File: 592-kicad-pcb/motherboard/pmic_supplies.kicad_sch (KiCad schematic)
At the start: 0 parts

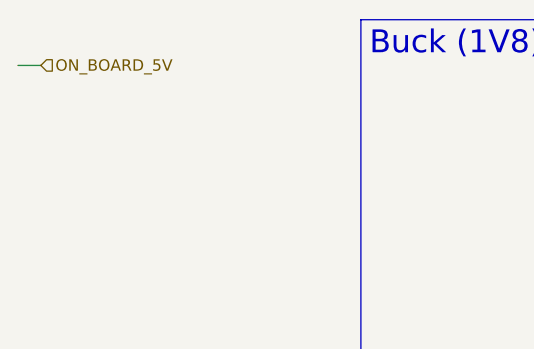
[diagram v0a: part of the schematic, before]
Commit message: pmic switching schem done
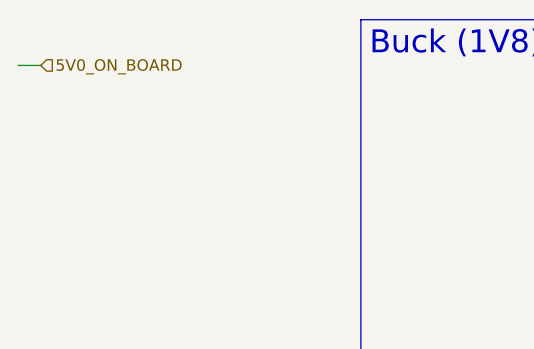
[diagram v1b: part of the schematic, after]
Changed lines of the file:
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@@
 		)
 	)
-	(hierarchical_label "ON_BOARD_5V"
+	(hierarchical_label "5V0_ON_BOARD"
 		(shape input)
 		(at 29.21 27.94 0)

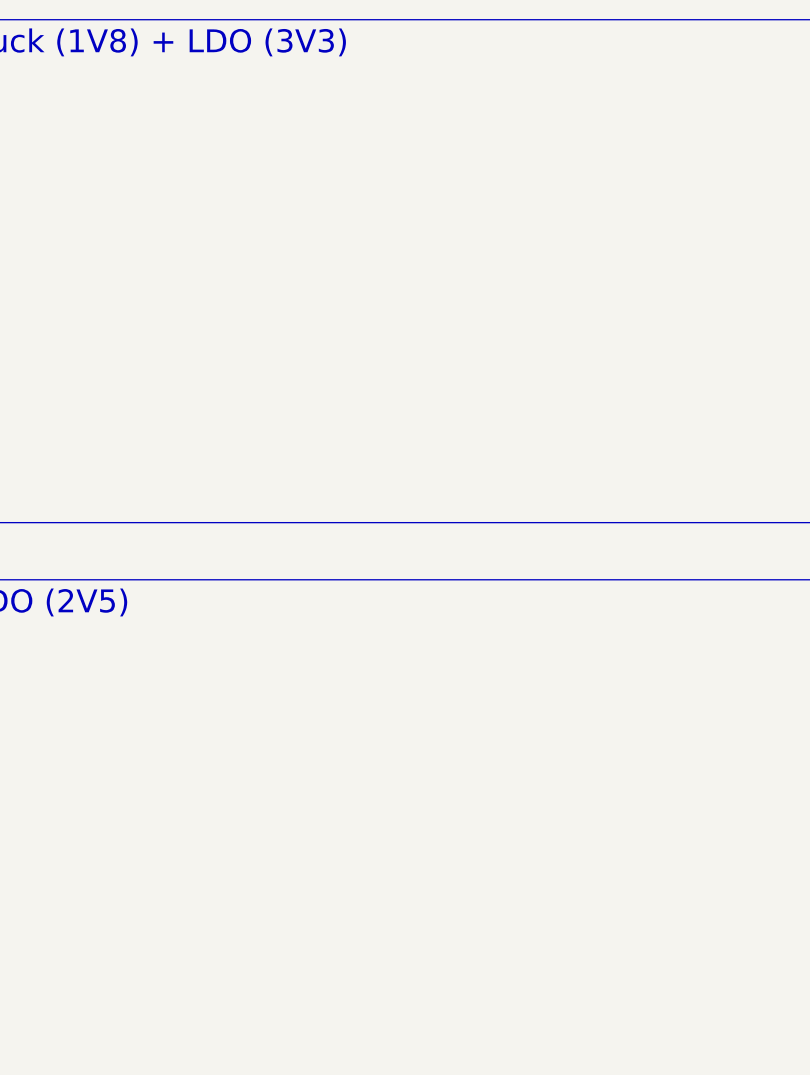
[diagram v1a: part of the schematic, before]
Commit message: 2V5 LDO symbol in its own dir
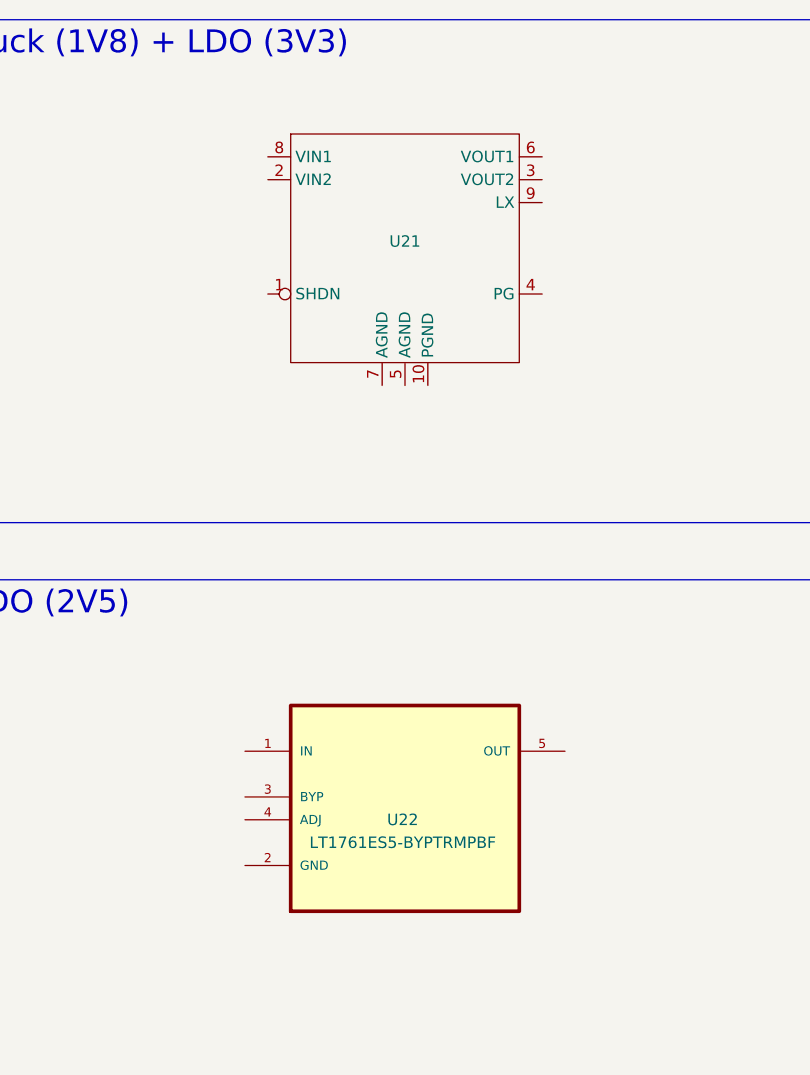
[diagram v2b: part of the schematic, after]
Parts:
- added U21: ~, symbol 592-partslib:TC1304-VI0EMF
- added U22: LT1761ES5-BYPTRMPBF, LT1761ES5-BYPTRMPBF:SOT95P280X145-5N, symbol LT1761ES5-BYPTRMPBF:LT1761ES5-BYPTRMPBF
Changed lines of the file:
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@@
+		)
+	)
+	(symbol
+		(lib_id "LT1761ES5-BYPTRMPBF:LT1761ES5-BYPTRMPBF")
+		(at 114.3 106.68 0)
+		(unit 1)
+		(exclude_from_sim no)
+		(in_bom yes)
+		(on_board yes)
+		(dnp no)
+		(property "Reference" "U22"
+			(at 114.046 111.76 0)
+			(effects
+				(font
+					(size 1.27 1.27)
+				)
+			)
+		)
+		(property "Value" "LT1761ES5-BYPTRMPBF"
+			(at 114.046 114.3 0)
+			(effects
+				(font
+					(size 1.27 1.27)
+				)
+			)
+		)
+		(property "Footprint" "LT1761ES5-BYPTRMPBF:SOT95P280X145-5N"
+			(at 114.3 106.68 0)
+			(effects
+				(font
+					(size 1.27 1.27)
+				)
+				(justify bottom)
+				(hide yes)
+			)
+		)
+		(property "Datasheet" ""
+			(at 114.3 106.68 0)
+			(effects
+				(font
+					(size 1.27 1.27)
+				)
+				(hide yes)
+			)
+		)
+		(property "Description" ""
+			(at 114.3 106.68 0)
+			(effects
+				(font
+					(size 1.27 1.27)
+				)
+				(hide yes)
+			)
+		)
+		(property "MPN" "LT1761ES5-BYP#TRMPBF"
+			(at 114.3 106.68 0)
+			(effects
+				(font
+					(size 1.27 1.27)
+				)
+				(justify bottom)
+				(hide yes)
+			)
+		)
+		(property "SUPPLIER" "Linear Technology"
+			(at 114.3 106.68 0)
+			(effects
+				(font
+					(size 1.27 1.27)
+				)
+				(justify bottom)
+				(hide yes)
+			)
+		)
+		(property "OC_NEWARK" "19P0914"
+			(at 114.3 106.68 0)
+			(effects
+				(font
+					(size 1.27 1.27)
+				)
+				(justify bottom)
+				(hide yes)
+			)
+		)
+		(property "OC_FARNELL" "1663782"
+			(at 114.3 106.68 0)
+			(effects
+				(font
+					(size 1.27 1.27)
+				)
+				(justify bottom)
+				(hide yes)
+			)
+		)
+		(property "PACKAGE" "SOT-23-5"
+			(at 114.3 106.68 0)
+			(effects
+				(font
+					(size 1.27 1.27)
+				)
+				(justify bottom)
+				(hide yes)
+			)
+		)
+		(pin "4"
+		)
+		(pin "1"
+		)
+		(pin "5"
+		)
+		(pin "3"
+		)
+		(pin "2"
+		)
+		(instances
+			(project ""
+				(path "/5b0c97ac-fa03-4db8-b41b-0eee32b6f55d/f049e4ad-bebe-4338-850a-2727de737ae9/5cd7239b-a735-4cd0-9e02-9ed9ef16f904"
+					(reference "U22")
+					(unit 1)
+				)
+			)
+		)
+	)
+	(symbol
+		(lib_id "592-partslib:TC1304-VI0EMF")
+		(at 114.3 48.26 0)
+		(unit 1)
+		(exclude_from_sim no)
+		(in_bom yes)
+		(on_board yes)
+		(dnp no)
+		(property "Reference" "U21"
+			(at 114.3 47.498 0)
+			(effects
+				(font
+					(size 1.27 1.27)
+				)
+			)
+		)
+		(property "Value" "~"
+			(at 114.3 50.038 0)
+			(effects
+				(font
+					(size 1.27 1.27)
+				)
+			)
+		)
+		(property "Footprint" ""
+			(at 114.3 48.26 0)
+			(effects
+				(font
+					(size 1.27 1.27)
+				)
+				(hide yes)
+			)
+		)
+		(property "Datasheet" "https://www.lcsc.com/datasheet/C635408.pdf"
+			(at 114.3 48.26 0)
+			(effects
+				(font
+					(size 1.27 1.27)
+				)
+				(hide yes)
+			)
+		)
+		(property "Description" "Microchip Buck + LDO"
+			(at 114.3 48.26 0)
+			(effects
+				(font
+					(size 1.27 1.27)
+				)
+				(hide yes)
+			)
+		)
+		(pin "7"
+		)
+		(pin "1"
+		)
+		(pin "6"
+		)
+		(pin "5"
+		)
+		(pin "8"
+		)
+		(pin "10"
+		)
+		(pin "2"
+		)
+		(pin "9"
+		)
+		(pin "4"
+		)
+		(pin "3"
+		)
+		(instances
+			(project ""
+				(path "/5b0c97ac-fa03-4db8-b41b-0eee32b6f55d/f049e4ad-bebe-4338-850a-2727de737ae9/5cd7239b-a735-4cd0-9e02-9ed9ef16f904"
+					(reference "U21")
+					(unit 1)
+				)
+			)
 		)
 	)

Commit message: 2V5 added to part lib (again?), supplies schem done?
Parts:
- added C36, C37: 4.7u, symbol Device:C_Small
- added C38, C39: 1u, symbol Device:C_Small
- added C40: 0.01u, symbol Device:C_Small
- added C41: 10u, symbol Device:C_Small
- added L1: 4.7u, symbol Device:L_Small
- added R58: 10k, symbol Device:R_Small
- U21: value ~ -> MICROCHIP TC1304-VI0EMF
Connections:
- net 5V0_ON_BOARD: now also U21.1 (SHDN), U21.2 (VIN2), U21.8 (VIN1), U22.1 (IN), U22.4 (SHDN), C36.2, C39.2, R58.1
- net GND: now reaches U22.2 (GND)
- net GND: now also C39.1, C41.1
- net BYP: now reaches U22.3 (BYP)
- net BYP: now also C40.1
- net 2V5_LDO: now reaches U22.5 (OUT)
- net 2V5_LDO: now also C40.2, C41.2
- net PGND: now reaches U21.10 (PGND)
- net PGND: now also C36.1, C37.2, C38.2
- net 3V3_LDO: now reaches U21.3 (VOUT2)
- net 3V3_LDO: now also C38.1
- net PG: now reaches U21.4 (PG)
- net PG: now also R58.2
- net AGND: now reaches U21.5 (AGND)
- net AGND: now also U21.7 (AGND)
- net 1V8_BUCK: now reaches U21.6 (VOUT1)
- net 1V8_BUCK: now also C37.1, L1.2
- net LX: now reaches U21.9 (LX)
- net LX: now also L1.1
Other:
- note added: "Buck : Vout1 : MGMT & USER DIG LDO : Vout2 : MGMT & USER ANA"
- note added: "SHDN detects from Vin for auto enable of outputs"
- moved on the sheet: U22

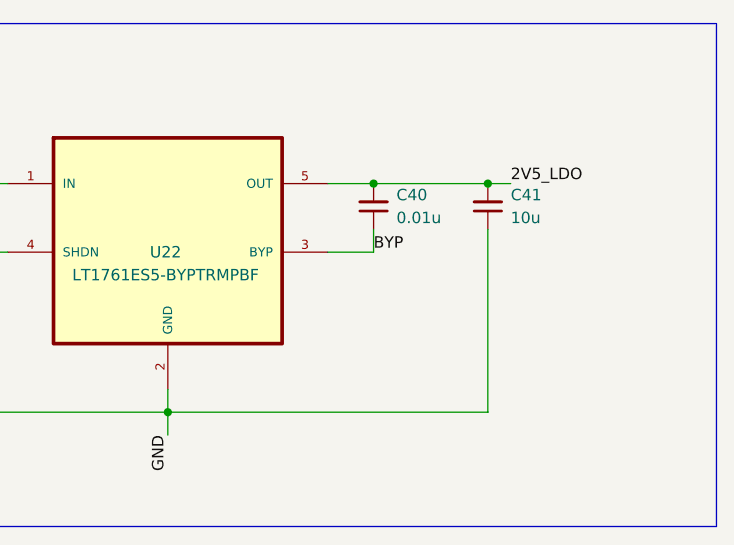
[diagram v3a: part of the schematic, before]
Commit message: note on bypass cap on schem
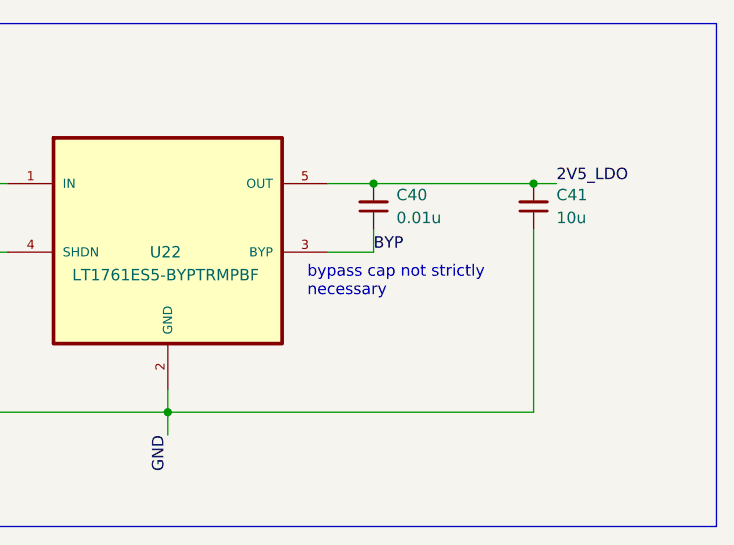
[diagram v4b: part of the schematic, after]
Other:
- note added: "bypass cap not strictly necessary"
- moved on the sheet: C41
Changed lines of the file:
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@@
+		)
+	)
+	(text "bypass cap not strictly\nnecessary"
+		(exclude_from_sim no)
+		(at 129.794 115.062 0)
+		(effects
+			(font
+				(size 1.27 1.27)
+			)
+			(justify left)
 		)
 	)
@@
 	)
 	(junction
-		(at 149.86 104.14)
+		(at 154.94 104.14)
 		(diameter 0)
 		(color 0 0 0 0)
@@
 	(wire
 		(pts
+			(xy 137.16 104.14) (xy 154.94 104.14)
+		)
+		(stroke
+			(width 0)
+			(type default)
+		)
+	)
+	(wire
+		(pts
 			(xy 137.16 109.22) (xy 137.16 111.76)
 		)
@@
 	(wire
 		(pts
-			(xy 137.16 104.14) (xy 149.86 104.14)
-		)
-		(stroke
-			(width 0)
-			(type default)
-		)
-	)
-	(wire
-		(pts
 			(xy 86.36 129.54) (xy 114.3 129.54)
 		)
@@
 	(wire
 		(pts
-			(xy 114.3 129.54) (xy 149.86 129.54)
-		)
-		(stroke
-			(width 0)
-			(type default)
-		)
-	)
-	(wire
-		(pts
 			(xy 147.32 43.18) (xy 147.32 40.64)
 		)
@@
 	(wire
 		(pts
-			(xy 149.86 109.22) (xy 149.86 129.54)
+			(xy 154.94 109.22) (xy 154.94 129.54)
 		)
 		(stroke
@@
 	(wire
 		(pts
-			(xy 149.86 104.14) (xy 152.4 104.14)
+			(xy 154.94 104.14) (xy 157.48 104.14)
 		)
 		(stroke
@@
 		(pts
 			(xy 137.16 111.76) (xy 132.08 111.76)
+		)
+		(stroke
+			(width 0)
+			(type default)
+		)
+	)
+	(wire
+		(pts
+			(xy 114.3 129.54) (xy 154.94 129.54)
 		)
 		(stroke
@@
 	)
 	(label "2V5_LDO"
-		(at 152.4 104.14 0)
+		(at 157.48 104.14 0)
 		(effects
 			(font
@@
 	(symbol
 		(lib_id "Device:C_Small")
-		(at 149.86 106.68 180)
+		(at 154.94 106.68 180)
 		(unit 1)
 		(exclude_from_sim no)
@@
 		(dnp no)
 		(property "Reference" "C41"
-			(at 152.4 105.4035 0)
+			(at 157.48 105.4035 0)
 			(effects
 				(font
@@
 		)
 		(property "Value" "10u"
-			(at 152.4 107.9435 0)
+			(at 157.48 107.9435 0)
 			(effects
 				(font
@@
 		)
 		(property "Footprint" ""
-			(at 149.86 106.68 0)
+			(at 154.94 106.68 0)
 			(effects
 				(font
@@
 		)
 		(property "Datasheet" "~"
-			(at 149.86 106.68 0)
+			(at 154.94 106.68 0)
 			(effects
 				(font
@@
 		)
 		(property "Description" "Unpolarized capacitor, small symbol"
-			(at 149.86 106.68 0)
-			(effects
-				(font
+			(at 154.94 106.68 0)
+			(effects
+				(font
